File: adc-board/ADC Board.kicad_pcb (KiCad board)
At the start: 4 copper layers, 99 x 66 mm, 118 parts, among them J1 ST-LINK/V2, J2 Sensors, J3 USART1, J4 USART6, J5 UE27AC5410H, J6 54601-908WPLF, U1 STM32H743ZITx, U10 MCP1501T-30E/SN, U11 AP7361C-33E-13, U12 AP7361C-33E-13, U13 P78E05-1000, U14 ISL83490, U3 USBLC6-2SC6, U4 AD8544, U5 AD8544, U6 AD8544, U7 AD8544, U8 AD8544, U9 AD8544, Y1 NX3225GD-8.000M-EXS00A-CG04874

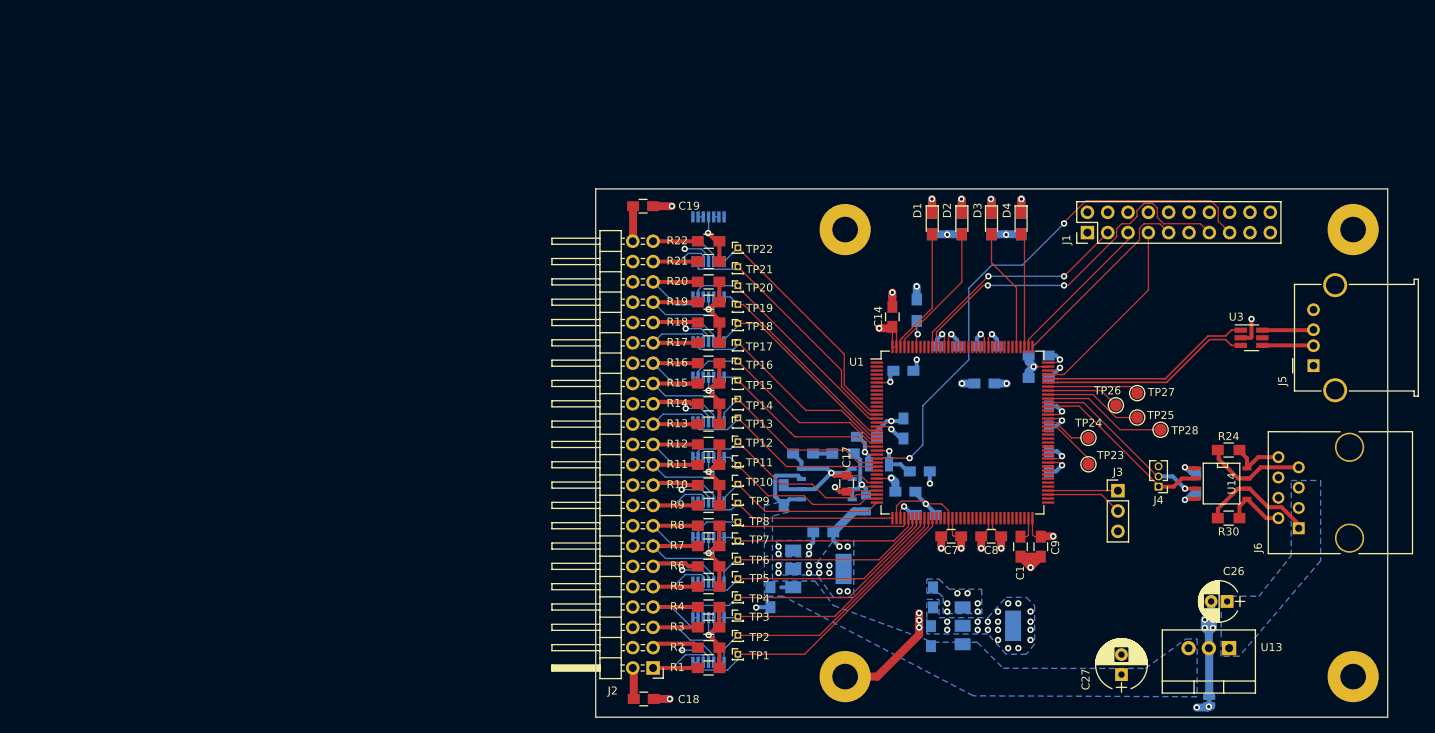
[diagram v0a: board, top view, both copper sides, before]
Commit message: adc board schematic tweaks and complete relayout
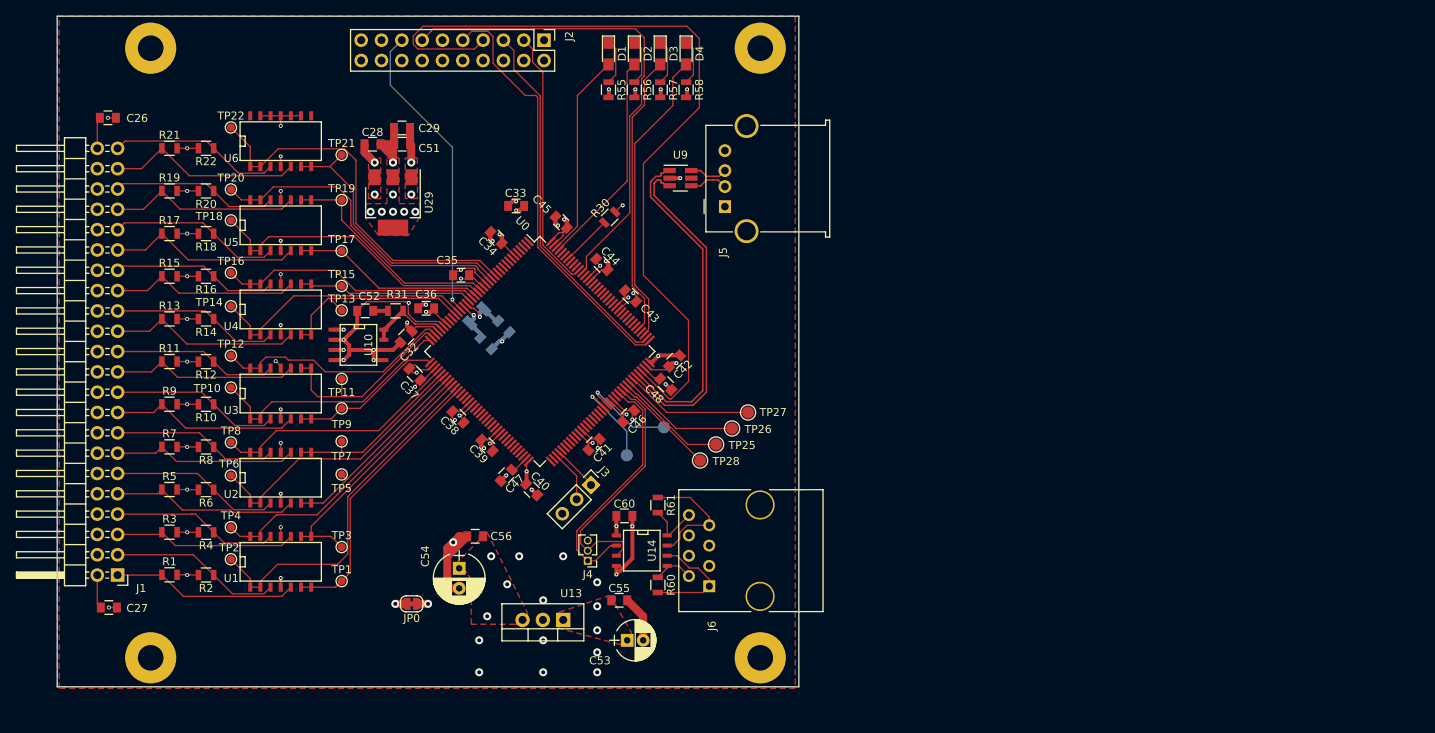
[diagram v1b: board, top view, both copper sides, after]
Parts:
- removed C1, C2, C20, C21: 2.2uF, Capacitors_SMD:C_0805_HandSoldering
- removed C10: DC84, Capacitors_SMD:C_0805_HandSoldering
- removed C11: DC108, Capacitors_SMD:C_0805_HandSoldering
- removed C12: DC121, Capacitors_SMD:C_0805_HandSoldering
- removed C13: DC131, Capacitors_SMD:C_0805_HandSoldering
- removed C14: DC144, Capacitors_SMD:C_0805_HandSoldering
- removed C15: DC95, Capacitors_SMD:C_0805_HandSoldering
- removed C16, C22, C23, C24, C25: 4.7uF, Capacitors_SMD:C_0805_HandSoldering
- removed C17: DC33, Capacitors_SMD:C_0805
- removed C18, C19: 1uF, Capacitors_SMD:C_0805_HandSoldering
- removed C3: DC6, Capacitors_SMD:C_0805_HandSoldering
- removed C30: 4.3pF, Capacitors_SMD:C_0805_HandSoldering
- removed C31: DC32, Capacitors_SMD:C_0805
- removed C4: DC17, Capacitors_SMD:C_0805_HandSoldering
- removed C5: DC30, Capacitors_SMD:C_0805_HandSoldering
- removed C6: DC39, Capacitors_SMD:C_0805_HandSoldering
- removed C7: DC52, Capacitors_SMD:C_0805_HandSoldering
- removed C8: DC62, Capacitors_SMD:C_0805_HandSoldering
- removed C9: DC72, Capacitors_SMD:C_0805_HandSoldering
- removed R23: 50, Resistors_SMD:R_0805_HandSoldering
- removed R24: 120, Resistors_SMD:R_0805_HandSoldering
- removed R25, R26, R27, R28: CL, Resistors_SMD:R_0805_HandSoldering
- removed R29: 10k, Resistors_SMD:R_0805_HandSoldering
- removed U11, U12: AP7361C-33E-13, TO_SOT_Packages_SMD:SOT-223-3_TabPin2
- removed U7, U8: AD8544, SMD_Packages:SSOP-14
- added C32: DC33, Capacitors_SMD:C_0805, F.Cu at (75.4, 87.1)
- added C33: 4.7uF, Capacitors_SMD:C_0805, F.Cu at (89.1, 70.7)
- added C34: DC6, Capacitors_SMD:C_0805, F.Cu at (86.6, 74.7)
- added C35: DC17, Capacitors_SMD:C_0805, F.Cu at (82.2, 79.4)
- added C36: DC30, Capacitors_SMD:C_0805, F.Cu at (77.9, 83.5)
- added C37: DC39, Capacitors_SMD:C_0805, F.Cu at (76.5, 91.8)
- added C38: DC52, Capacitors_SMD:C_0805, F.Cu at (81.9, 97.1)
- added C39: DC62, Capacitors_SMD:C_0805, F.Cu at (85.5, 100.6)
- added C40: DC72, Capacitors_SMD:C_0805, F.Cu at (91.1, 106.2)
- added C41: DC84, Capacitors_SMD:C_0805, F.Cu at (98.9, 100.5)
- added C42: DC108, Capacitors_SMD:C_0805, F.Cu at (108.9, 90.1)
- added C43: DC121, Capacitors_SMD:C_0805, F.Cu at (103.4, 82.0)
- added C44: DC131, Capacitors_SMD:C_0805, F.Cu at (99.8, 78.0)
- added C45: DC144, Capacitors_SMD:C_0805, F.Cu at (94.7, 72.7)
- added C46: DC95, Capacitors_SMD:C_0805, F.Cu at (103.2, 97.0)
- added C47: 2.2uF, Capacitors_SMD:C_0805, F.Cu at (87.9, 104.4)
- added C48: 2.2uF, Capacitors_SMD:C_0805, F.Cu at (107.8, 93.0)
- added C49: 4.3pF, Capacitors_SMD:C_0805, B.Cu at (87.6, 85.8)
- added C50: 4.3pF, Capacitors_SMD:C_0805, B.Cu at (85.3, 87.9)
- added C51: 2.2uF, Capacitors_SMD:C_0805, F.Cu at (74.9, 63.0)
- added C52: 2.2uF, Capacitors_SMD:C_0805, F.Cu at (70.2, 83.8)
- added C53: 10uF EEA-GA1V100, Capacitors_THT:CP_Radial_D5.0mm_P2.00mm, F.Cu at (103.0, 125.0)
- added C54: 22uF ECE-A1HKA220, Capacitors_THT:CP_Radial_D6.3mm_P2.50mm, F.Cu at (82.0, 116.0)
- added C55: DC, Capacitors_SMD:C_0805, F.Cu at (102.0, 120.0)
- added C56: DC, Capacitors_SMD:C_0805, F.Cu at (84.0, 112.0)
- added C60: DC, Capacitors_SMD:C_0805, F.Cu at (102.7, 109.4)
- added R31: 50, Resistors_SMD:R_0805, F.Cu at (74.0, 83.8)
- added R55: CL, Resistors_SMD:R_0805, F.Cu at (100.7, 56.2)
- added R56: CL, Resistors_SMD:R_0805, F.Cu at (103.9, 56.2)
- added R57: CL, Resistors_SMD:R_0805, F.Cu at (107.1, 56.2)
- added R58: CL, Resistors_SMD:R_0805, F.Cu at (110.4, 56.2)
- added R60: 120, Resistors_SMD:R_0805, F.Cu at (106.8, 118.1)
- added R61: 120, Resistors_SMD:R_0805, F.Cu at (106.8, 108.1)
- added U0: STM32H743ZITx, Housings_QFP:LQFP-144_20x20mm_Pitch0.5mm, F.Cu at (92.1, 88.9)
- added U2: Opamp_Quad_Generic, SMD_Packages:SOIC-14_N, F.Cu at (59.7, 104.5)
- added U29: AP7361C-33E-13, TO_SOT_Packages_SMD:SOT-223-3_TabPin2, F.Cu at (73.7, 70.3)
- C26: value 10uF EEA-GA1V100 -> 1uF; footprint Capacitors_THT:CP_Radial_D5.0mm_P2.00mm -> Capacitors_SMD:C_0805
- C27: value 22uF ECE-A1HKA220 -> 1uF; footprint Capacitors_THT:CP_Radial_D6.3mm_P2.50mm -> Capacitors_SMD:C_0805
- C28: value DC -> 4.7uF; footprint Capacitors_SMD:C_0805_HandSoldering -> Capacitors_SMD:C_0805; moved to F.Cu
- C29: value 4.3pF -> 4.7uF; footprint Capacitors_SMD:C_0805_HandSoldering -> Capacitors_SMD:C_0805; moved to F.Cu
- J1: value ST-LINK/V2 -> BHR-44-HUA; footprint Pin_Headers:Pin_Header_Straight_2x10_Pitch2.54mm -> Pin_Headers:Pin_Header_Angled_2x22_Pitch2.54mm
- J2: value Sensors -> ST-LINK/V2; footprint Pin_Headers:Pin_Header_Angled_2x22_Pitch2.54mm -> Pin_Headers:Pin_Header_Straight_2x10_Pitch2.54mm
- JP0, U10: moved to F.Cu
- R1, R10, R11, R12, R13, R14, R15, R16, R17, R18, R19, R2, R20, R21, R22, R3, R4, R5, R6, R7, R8, R9: footprint Resistors_SMD:R_0805_HandSoldering -> Resistors_SMD:R_0805
- R30: value 120 -> 10k; footprint Resistors_SMD:R_0805_HandSoldering -> Resistors_SMD:R_0805
- TP1, TP10, TP11, TP12, TP13, TP14, TP15, TP16, TP17, TP18, TP19, TP2, TP20, TP21, TP22, TP3, TP4, TP5, TP6, TP7, TP8, TP9: footprint Pin_Headers:Pin_Header_Straight_1x01_Pitch1.00mm -> Testpoint:TestPoint_Pad_D1.0mm
- TP23, TP24: moved to B.Cu
- U1: value STM32H743ZITx -> Opamp_Quad_Generic; footprint Housings_QFP:LQFP-144_20x20mm_Pitch0.5mm -> SMD_Packages:SOIC-14_N
- U13: value P78E05-1000 -> 3.3V Reg
- U3: value USBLC6-2SC6 -> Opamp_Quad_Generic; footprint TO_SOT_Packages_SMD:SOT-23-6_Handsoldering -> SMD_Packages:SOIC-14_N
- U4, U5, U6: value AD8544 -> Opamp_Quad_Generic; footprint SMD_Packages:SSOP-14 -> SMD_Packages:SOIC-14_N; moved to F.Cu
- U9: value AD8544 -> USBLC6-2SC6; footprint SMD_Packages:SSOP-14 -> TO_SOT_Packages_SMD:SOT-23-6_Handsoldering; moved to F.Cu
- moved C26 152.4 mm to (38.1, 59.7)
- moved J1 128.6 mm to (39.3, 116.8), turned to 180 degrees
- moved C27 126.9 mm to (38.2, 120.9), turned to 180 degrees
- moved U3 121.5 mm to (59.7, 94.0)
- moved H1 117.1 mm to (43.4, 51.0)
- moved C28 111.3 mm to (71.2, 63.0), turned to 0 degrees
- moved H2 108.0 mm to (119.6, 51.0)
- moved H4 102.0 mm to (43.4, 127.2)
- moved JP0 100.4 mm to (76.1, 120.4), turned to 180 degrees
- moved H3 91.4 mm to (119.6, 127.2)
- moved U1 86.7 mm to (59.7, 115.1)
- moved R30 86.0 mm to (100.8, 72.1), turned to 45 degrees
- moved U13 83.3 mm to (95.0, 122.5)
- moved J2 79.6 mm to (92.6, 50.0), turned to 270 degrees
- moved C29 77.7 mm to (74.9, 61.0)
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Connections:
- C26 pad 1: +12V -> GNDA
- C26 pad 2: GNDD -> +3.3VA
- C27 pad 1: +5V -> GNDA
- C27 pad 2: GNDD -> +3.3VA
- C28 pad 1: +3V3 -> +3.3VA
- C28 pad 2: GNDD -> GNDA
- C29 pad 1: GNDD -> +5V
- C29 pad 2: Net-(C29-Pad2) -> GNDA
- J1 pad 1: Net-(J1-Pad1) -> /Analog Input/Sen1R
- J1 pad 10: GNDD -> +3.3VA
- J1 pad 11: Net-(J1-Pad11) -> /Analog Input/Sen6R
- J1 pad 12: GNDD -> +3.3VA
- J1 pad 13: /JTDO -> /Analog Input/Sen7R
- J1 pad 14: GNDD -> +3.3VA
- J1 pad 15: /NRST -> /Analog Input/Sen8R
- J1 pad 16: GNDD -> +3.3VA
- J1 pad 17: Net-(J1-Pad17) -> /Analog Input/Sen9R
- J1 pad 18: GNDD -> +3.3VA
- J1 pad 19: Net-(J1-Pad19) -> /Analog Input/Sen10R
- J1 pad 2: Net-(J1-Pad2) -> +3.3VA
- J1 pad 20: GNDD -> +3.3VA
- J1 pad 3: /JNTRST -> /Analog Input/Sen2R
- J1 pad 4: GNDD -> +3.3VA
- J1 pad 5: /JTDI -> /Analog Input/Sen3R
- J1 pad 6: GNDD -> +3.3VA
- J1 pad 7: /JTMS -> /Analog Input/Sen4R
- J1 pad 8: GNDD -> +3.3VA
- J1 pad 9: /JTCK -> /Analog Input/Sen5R
- J2 pad 1: /Sen1R -> (no net)
- J2 pad 10: +3.3VA -> GNDD
- J2 pad 11: /Sen6R -> (no net)
- J2 pad 12: +3.3VA -> GNDD
- J2 pad 13: /Sen7R -> /JTDO
- J2 pad 14: +3.3VA -> GNDD
- J2 pad 15: /Sen8R -> /NRST
- J2 pad 16: +3.3VA -> GNDD
- J2 pad 17: /Sen9R -> (no net)
- J2 pad 18: +3.3VA -> GNDD
- J2 pad 19: /Sen10R -> (no net)
- J2 pad 2: +3.3VA -> (no net)
- J2 pad 20: +3.3VA -> GNDD
- J2 pad 3: /Sen2R -> /JNTRST
- J2 pad 4: +3.3VA -> GNDD
- J2 pad 5: /Sen3R -> /JTDI
- J2 pad 6: +3.3VA -> GNDD
- J2 pad 7: /Sen4R -> /JTMS
- J2 pad 8: +3.3VA -> GNDD
- J2 pad 9: /Sen5R -> /JTCK
- J5 pad 1: Net-(J5-Pad1) -> (no net)
- J6 pad 3: +12V -> +5V
- J6 pad 5: +12V -> +5V
- R1 pad 1: /Sen1R -> /Analog Input/Sen1R
- R10 pad 1: /Sen10R -> /Analog Input/Sen10R
- R11 pad 1: /Sen11R -> /Analog Input/Sen11R
- R12 pad 1: /Sen12R -> /Analog Input/Sen12R
- R13 pad 1: /Sen13R -> /Analog Input/Sen13R
- R14 pad 1: /Sen14R -> /Analog Input/Sen14R
- R15 pad 1: /Sen15R -> /Analog Input/Sen15R
- R16 pad 1: /Sen16R -> /Analog Input/Sen16R
- R17 pad 1: /Sen17R -> /Analog Input/Sen17R
- R18 pad 1: /Sen18R -> /Analog Input/Sen18R
- R19 pad 1: /Sen19R -> /Analog Input/Sen19R
- R2 pad 1: /Sen2R -> /Analog Input/Sen2R
- R20 pad 1: /Sen20R -> /Analog Input/Sen20R
- R21 pad 1: /Sen21R -> /Analog Input/Sen21R
- R22 pad 1: /Sen22R -> /Analog Input/Sen22R
- R3 pad 1: /Sen3R -> /Analog Input/Sen3R
- R30 pad 1: /RS485/Z -> /BOOT0
- R30 pad 2: /RS485/Y -> GNDD
- R4 pad 1: /Sen4R -> /Analog Input/Sen4R
- R5 pad 1: /Sen5R -> /Analog Input/Sen5R
- R6 pad 1: /Sen6R -> /Analog Input/Sen6R
- R7 pad 1: /Sen7R -> /Analog Input/Sen7R
- R8 pad 1: /Sen8R -> /Analog Input/Sen8R
- R9 pad 1: /Sen9R -> /Analog Input/Sen9R
- U1 pad 1: Net-(U1-Pad1) -> /Sen2
- U1 pad 10: Net-(U1-Pad10) -> /Analog Input/Sen3R
- U1 pad 11: Net-(U1-Pad11) -> GNDA
- U1 pad 12: Net-(U1-Pad12) -> /Analog Input/Sen4R
- U1 pad 13: /Sen22 -> /Sen4
- U1 pad 14: /Sen21 -> /Sen4
- U1 pad 2: Net-(U1-Pad2) -> /Sen2
- U1 pad 3: Net-(U1-Pad3) -> /Analog Input/Sen2R
- U1 pad 4: Net-(U1-Pad4) -> +3.3VA
- U1 pad 5: Net-(U1-Pad5) -> /Analog Input/Sen1R
- U1 pad 6: +3V3 -> /Sen1
- U1 pad 7: Net-(U1-Pad7) -> /Sen1
- U1 pad 8: Net-(U1-Pad8) -> /Sen3
- U1 pad 9: Net-(U1-Pad9) -> /Sen3
- U13 pad 1: +12V -> +5V
- U13 pad 3: +5V -> +3V3
- U3 pad 1: /USB_OTG_FS_D+ -> /Sen10
- U3 pad 2: GNDD -> /Sen10
- U3 pad 3: /USB_OTG_FS_D- -> /Analog Input/Sen10R
- U3 pad 4: /USB_D- -> +3.3VA
- U3 pad 5: Net-(U3-Pad5) -> /Analog Input/Sen9R
- U3 pad 6: /USB_D+ -> /Sen9
- U4 pad 1: /Sen2 -> /Sen14
- U4 pad 10: /Sen4R -> /Analog Input/Sen15R
- U4 pad 12: /Sen3R -> /Analog Input/Sen16R
- U4 pad 13: /Sen3 -> /Sen16
- U4 pad 14: /Sen3 -> /Sen16
- U4 pad 2: /Sen2 -> /Sen14
- U4 pad 3: /Sen2R -> /Analog Input/Sen14R
- U4 pad 5: /Sen1R -> /Analog Input/Sen13R
- U4 pad 6: /Sen1 -> /Sen13
- U4 pad 7: /Sen1 -> /Sen13
- U4 pad 8: /Sen4 -> /Sen15
- U4 pad 9: /Sen4 -> /Sen15
- U5 pad 1: /Sen6 -> /Sen18
- U5 pad 10: /Sen8R -> /Analog Input/Sen19R
- U5 pad 12: /Sen7R -> /Analog Input/Sen20R
- U5 pad 13: /Sen7 -> /Sen20
- U5 pad 14: /Sen7 -> /Sen20
- U5 pad 2: /Sen6 -> /Sen18
- U5 pad 3: /Sen6R -> /Analog Input/Sen18R
- U5 pad 5: /Sen5R -> /Analog Input/Sen17R
- U5 pad 6: /Sen5 -> /Sen17
- U5 pad 7: /Sen5 -> /Sen17
- U5 pad 8: /Sen8 -> /Sen19
- U5 pad 9: /Sen8 -> /Sen19
- U6 pad 1: /Sen10 -> /Sen22
- U6 pad 10: /Sen12R -> GNDA
- U6 pad 12: /Sen11R -> GNDA
- U6 pad 13: /Sen11 -> GNDA
- U6 pad 14: /Sen11 -> (no net)
- U6 pad 2: /Sen10 -> /Sen22
- U6 pad 3: /Sen10R -> /Analog Input/Sen22R
- U6 pad 5: /Sen9R -> /Analog Input/Sen21R
- U6 pad 6: /Sen9 -> /Sen21
- U6 pad 7: /Sen9 -> /Sen21
- U6 pad 8: /Sen12 -> (no net)
- U6 pad 9: /Sen12 -> GNDA
- U9 pad 1: /Sen22 -> /USB_OTG_FS_D+
- U9 pad 2: /Sen22 -> GNDD
- U9 pad 3: /Sen22R -> /USB_OTG_FS_D-
- U9 pad 4: +3.3VA -> /USB_D-
- U9 pad 5: /Sen21R -> (no net)
- U9 pad 6: /Sen21 -> /USB_D+
- Y1 pad 1: Net-(C29-Pad2) -> Net-(C49-Pad2)
- Y1 pad 2: Net-(C30-Pad2) -> Net-(C50-Pad2)
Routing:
- net /JTMS: track 24.1 -> 103.7 mm
- net /NRST: track 68.2 -> 37.9 mm, vias 2 -> 1
- net /JTCK: track 24.7 -> 53.2 mm
- net /JTDI: track 19.5 -> 46.2 mm
- net /Analog Input/Sen21R: track 0.00 -> 24.6 mm
- net /Analog Input/Sen17R: track 0.00 -> 24.3 mm
- net /Analog Input/Sen13R: track 0.00 -> 24.1 mm
- net /Analog Input/Sen19R: track 0.00 -> 24.0 mm
- net GNDD: track 108.6 -> 84.6 mm, vias 44 -> 37
- net /Analog Input/Sen9R: track 0.00 -> 23.8 mm
- net /Analog Input/Sen15R: track 0.00 -> 23.8 mm
- net /Analog Input/Sen5R: track 0.00 -> 23.5 mm
- net /Analog Input/Sen11R: track 0.00 -> 23.5 mm
- net /Analog Input/Sen1R: track 0.00 -> 23.3 mm
- net /Analog Input/Sen7R: track 0.00 -> 23.2 mm
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- added copper zone on F.Cu, net +3.3VA
- added copper zone on F.Cu, net +3V3
- added copper zone on F.Cu, net +5V
- added copper zone on F.Cu, net GNDA
- added copper zone on F.Cu, net GNDD
- removed copper zone on B.Cu, net +12V
- removed copper zone on B.Cu, net +3.3VA
- removed copper zone on B.Cu, net +3V3
- removed copper zone on B.Cu, net GNDA
- removed copper zone on B.Cu, net GNDD
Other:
- board size 99 x 66 mm -> 92.7 x 83.8 mm
- net class Default: clearance 0.18 -> 0.19; trace_width 0.16 -> 0.13; via_dia 0.8 -> 0.5; via_drill 0.41 -> 0.25
- rule trace_clearance: 0.18 -> 0.19
- rule trace_min: 0.16 -> 0.13
- rule via_min_drill: 0.41 -> 0.25
- rule via_min_size: 0.4 -> 0.5
- board text removed: "note the large holes on this receptable were modified. compare with amphenol data sheet"

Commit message: correct RS485 termination resistors, adjust ground pours
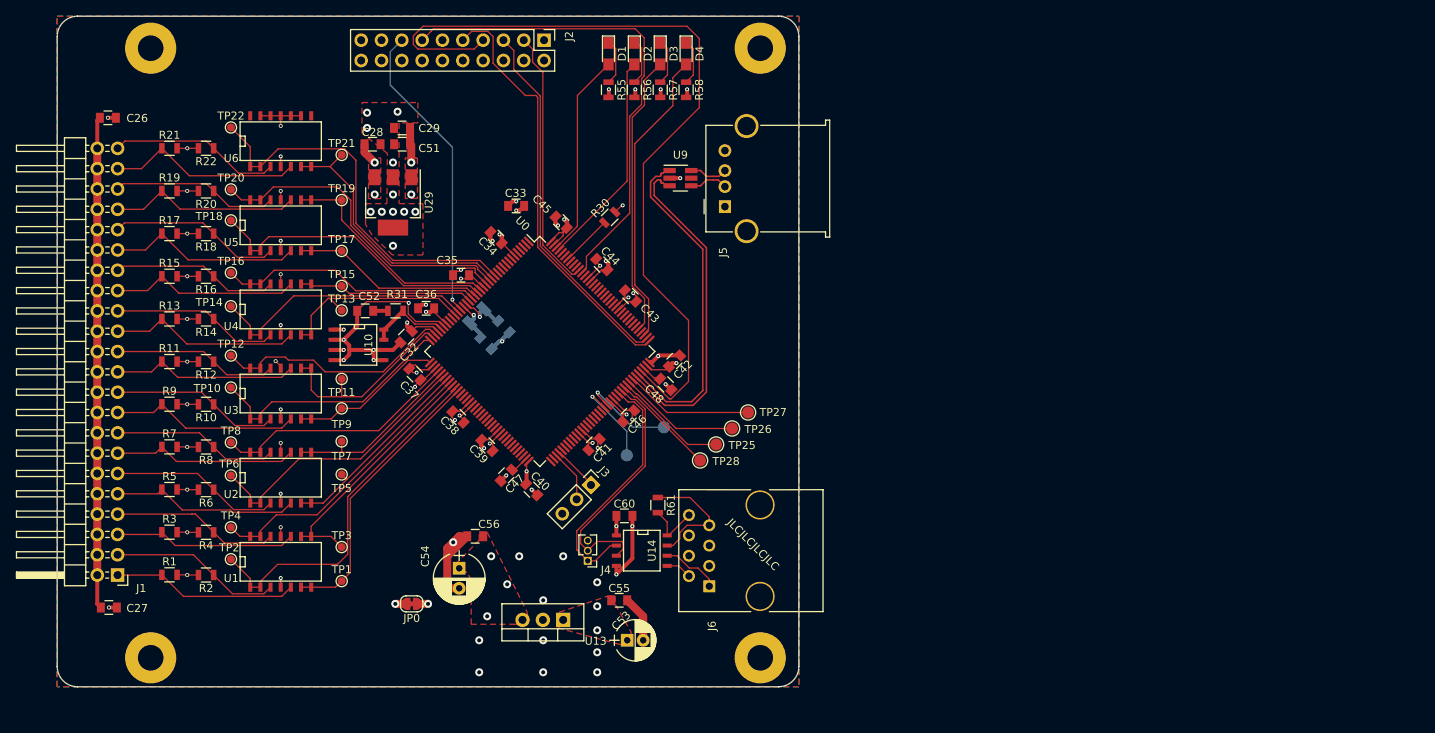
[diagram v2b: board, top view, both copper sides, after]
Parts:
- removed R60: 120, Resistors_SMD:R_0805
- R1, R10, R11, R12, R13, R14, R15, R16, R17, R18, R19, R2, R20, R21, R22, R3, R4, R5, R6, R7, R8, R9: value 2200 -> 1800
- U10: value MCP1501T-30E/SN -> MCP1501-20E/SN
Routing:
- net +3.3VA: track 23.4 -> 76.7 mm
- net GNDA: track 86.9 -> 77.9 mm, vias 32 -> 36
- net /RS485/Y: track 14.1 -> 7.35 mm
- net /RS485/Z: track 5.16 -> 3.25 mm
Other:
- outline, holes or cut-outs redrawn
- board text added: "JLCJLCJLCJLC"

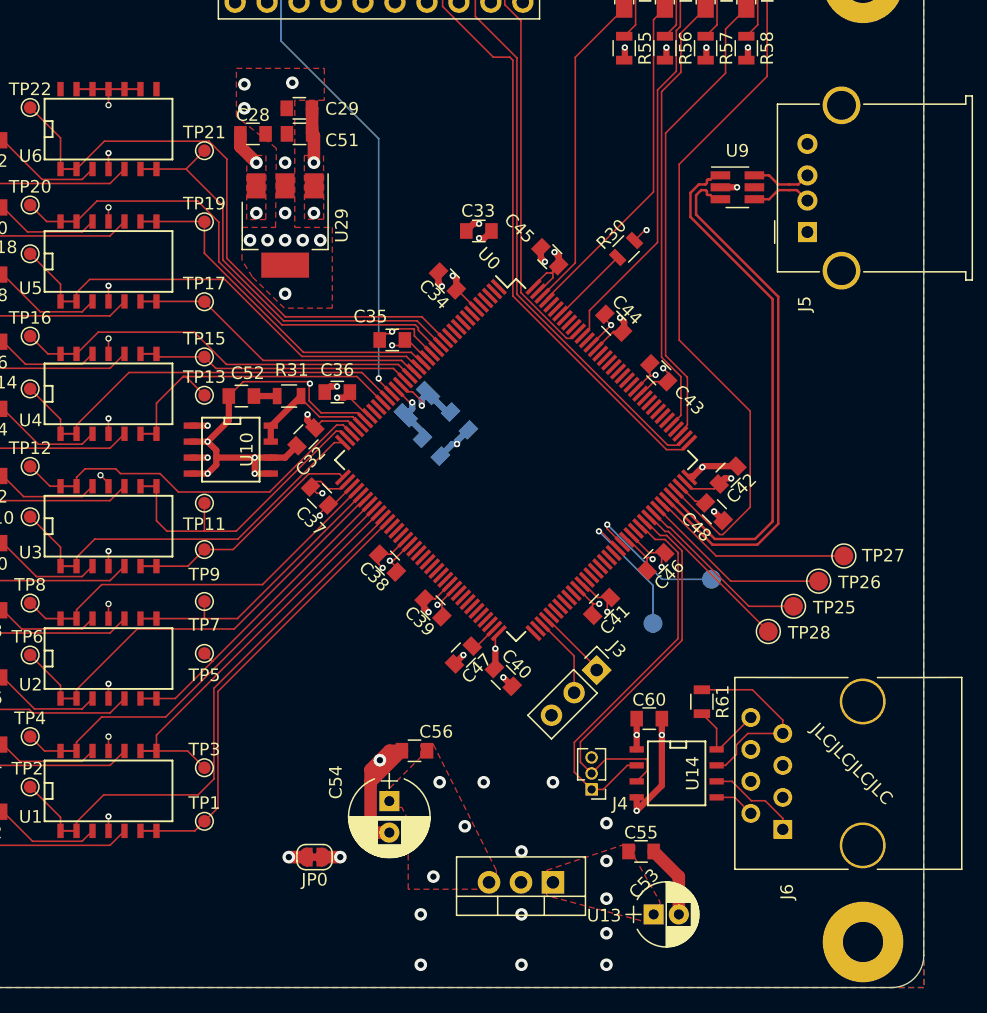
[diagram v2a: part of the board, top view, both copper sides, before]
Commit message: alternative power inputs; cap on NRST; 3.3V reg thermal work on PCB
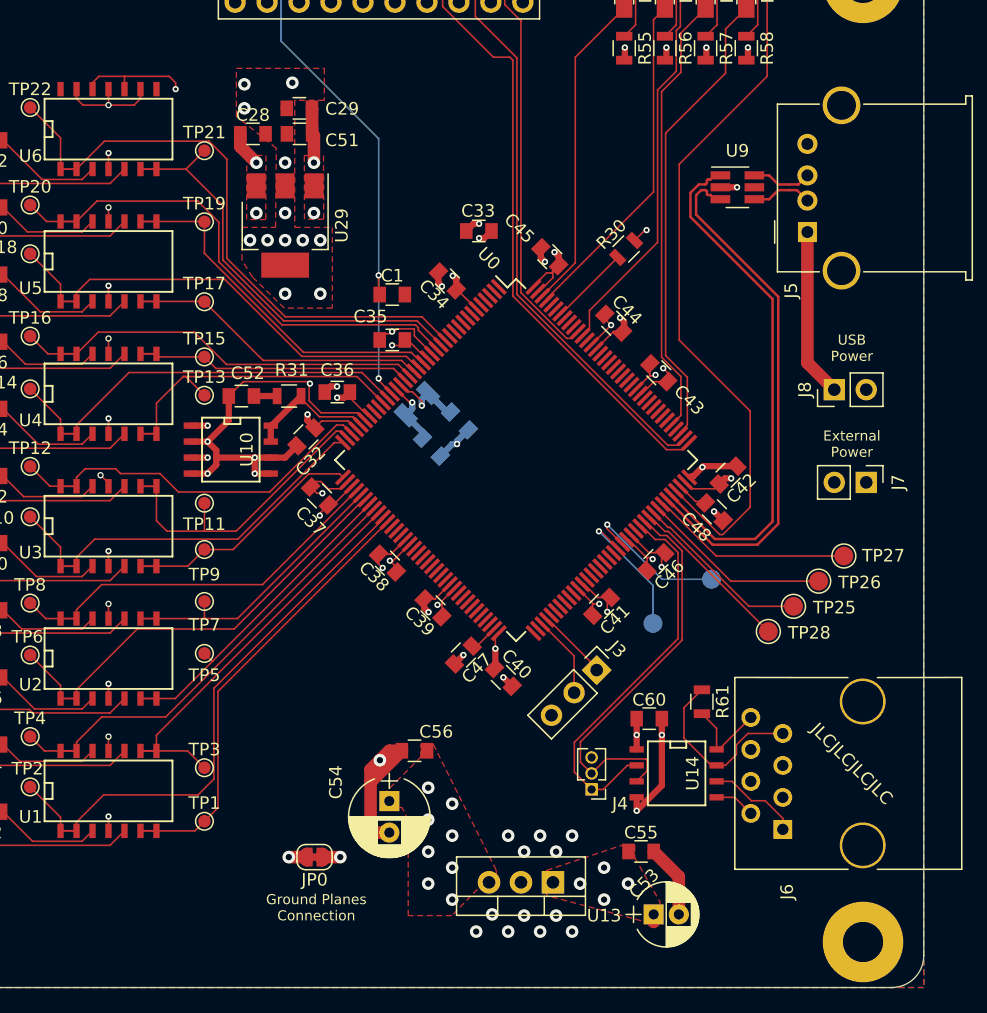
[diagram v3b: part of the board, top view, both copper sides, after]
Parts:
- added C1: 0.1uF, Capacitors_SMD:C_0805, F.Cu at (82.2, 75.8)
- added J7: AltPowerInput, Pin_Headers:Pin_Header_Straight_1x02_Pitch2.54mm, F.Cu at (119.9, 90.7)
- added J8: USBPowerJumper, Pin_Headers:Pin_Header_Straight_1x02_Pitch2.54mm, F.Cu at (117.3, 83.3)
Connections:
- J5 pad 1: (no net) -> Net-(J5-Pad1)
- U6 pad 10: GNDA -> +3.3VA
- U6 pad 12: GNDA -> +3.3VA
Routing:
- net Net-(J5-Pad1): track 0.00 -> 13.4 mm
- net +3.3VA: track 76.7 -> 85.8 mm, vias 9 -> 10
- net GNDA: track 77.9 -> 79.8 mm, vias 36 -> 37
- net /NRST: track 37.9 -> 39.4 mm, vias 1 -> 2
- net +5V: track 7.05 -> 7.66 mm, vias 6 -> 8
- net /RS485/B: track 15.2 -> 14.7 mm
- net GNDD: vias 37 -> 39
- net +3V3: vias 18 -> 23
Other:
- board text added: "External Power"
- board text added: "Ground Planes Connection"
- board text added: "USB Power"
